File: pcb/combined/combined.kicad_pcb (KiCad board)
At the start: 2 copper layers, 113.5 x 87.5 mm, 67 parts, among them J1 5V POWER, J10 PRESSURE, J11 XIAO D0-D6, J12 XIAO D7-5V, J2 MAINS_IN, J3 VALVE, J4 PUMP, J5 CAN BUS, J6 FLOW HALL, J8 BOILER SSR, Q1 SS8050, Q2 BT136S, Q3 SS8050, Q4 BT136S, Q5 AO3401A, Q6 2N7002, U1 MOC3043M, U2 MOC3023M, U3 EL817C, U4 TJA1051T/3, U5 TMP102AIDRLR, U6 ADS1115IDGSR

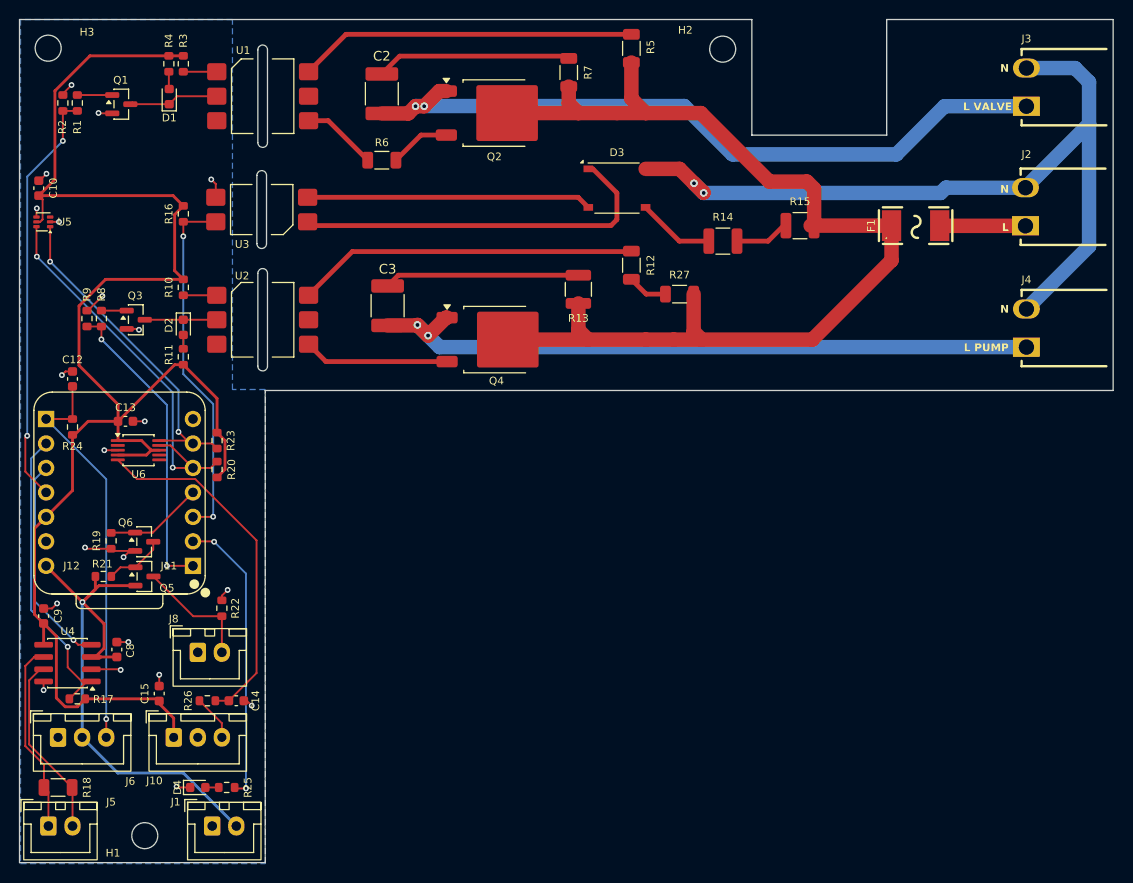
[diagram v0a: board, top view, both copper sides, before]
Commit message: small adjustment to combined PCB
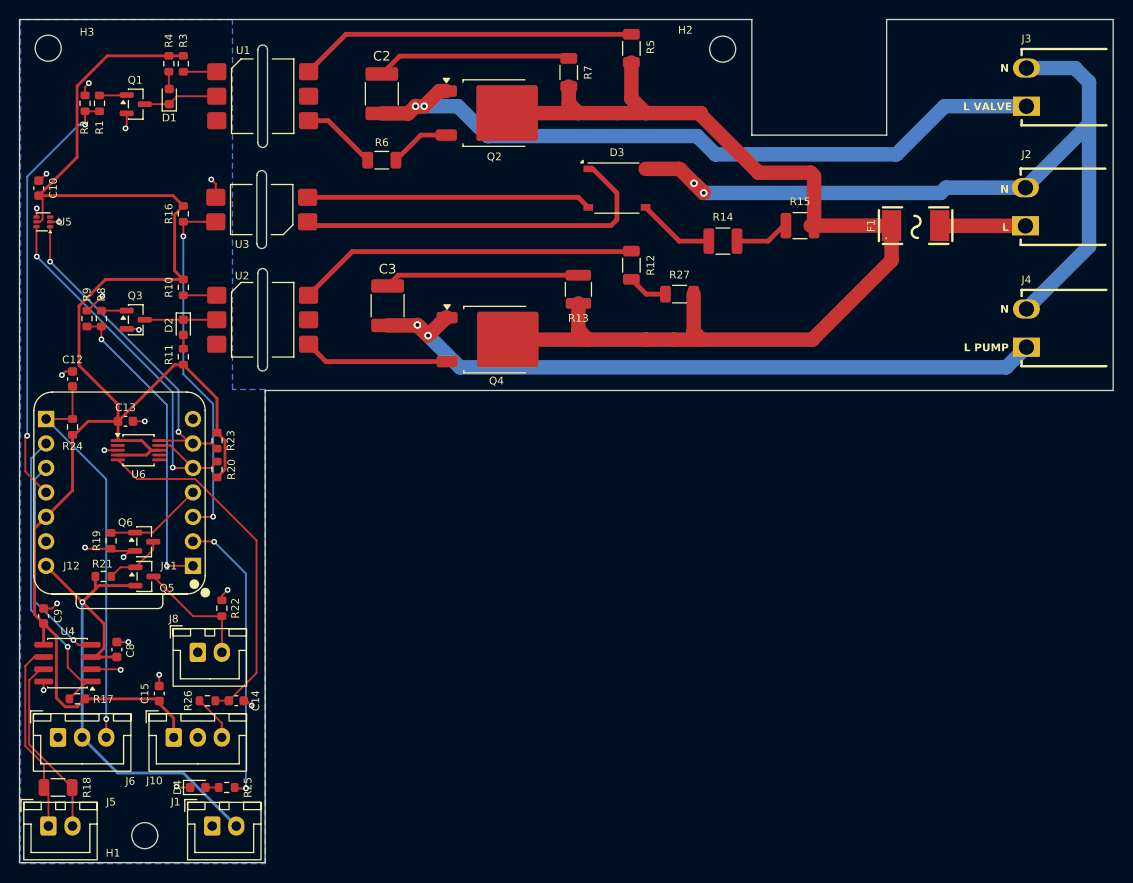
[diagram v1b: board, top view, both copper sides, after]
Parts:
- moved R1 2.30 mm to (88.8, 55.7)
- moved R2 2.30 mm to (87.3, 55.7)
- moved Q1 1.50 mm to (92.6, 55.8)
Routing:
- net Net-(D1-K): track 9.61 -> 7.81 mm
- net /L_PUMP: track 71.6 -> 73.3 mm
- net SSR: track 43.6 -> 44.9 mm
- net +3V3: track 166.1 -> 165.1 mm
- net /L: track 112.5 -> 113.3 mm
- net Net-(Q1-B): track 3.62 -> 2.84 mm
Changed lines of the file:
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@@
 	(footprint "Package_TO_SOT_SMD:SOT-23"
 		(layer "F.Cu")
-		(at 91.0625 55.7875)
+		(at 92.5625 55.7875)
 		(descr "SOT, 3 Pin (JEDEC TO-236 Var AB https://www.jedec.org/document_search?search_api_views_fulltext=TO-236)")
 		(tags "SOT TO_SOT_SMD")
@@
 	(footprint "Resistor_SMD:R_0603_1608Metric"
 		(layer "F.Cu")
-		(at 86.5 55.6625 90)
+		(at 88.8 55.7 90)
 		(descr "Resistor SMD 0603 (1608 Metric), square (rectangular) end terminal, IPC-7351 nominal, (Body size source: IPC-SM-782 page 72, https://www.pcb-3d.com/wordpress/wp-content/uploads/ipc-sm-782a_amendment_1_and_2.pdf)")
 		(tags "resistor")
@@
 	(footprint "Resistor_SMD:R_0603_1608Metric"
 		(layer "F.Cu")
-		(at 85 55.6625 90)
+		(at 87.3 55.7 90)
 		(descr "Resistor SMD 0603 (1608 Metric), square (rectangular) end terminal, IPC-7351 nominal, (Body size source: IPC-SM-782 page 72, https://www.pcb-3d.com/wordpress/wp-content/uploads/ipc-sm-782a_amendment_1_and_2.pdf)")
 		(tags "resistor")
@@
 	)
 	(segment
+		(start 91.625 58.175)
+		(end 91.5 58.3)
+		(width 0.2)
+		(layer "F.Cu")
+		(net "GND")
+	)
+	(segment
 		(start 100.87 64.07)
 		(end 100.4 63.6)
@@
 	)
 	(segment
-		(start 88.7375 56.7375)
-		(end 88.7 56.7)
-		(width 0.2)
-		(layer "F.Cu")
-		(net "GND")
-	)
-	(segment
 		(start 92.5 102.15)
 		(end 90.225 102.15)
@@
 	)
 	(segment
-		(start 85 54.8375)
-		(end 85 54.7)
-		(width 0.2)
-		(layer "F.Cu")
-		(net "GND")
-	)
-	(segment
 		(start 86 83.525)
 		(end 85.275 83.525)
@@
 	)
 	(segment
+		(start 87.3 54.875)
+		(end 87.3 54)
+		(width 0.2)
+		(layer "F.Cu")
+		(net "GND")
+	)
+	(segment
 		(start 83 115.7)
 		(end 83 116.6)
@@
 	)
 	(segment
-		(start 85 54.7)
-		(end 85.9 53.8)
-		(width 0.2)
-		(layer "F.Cu")
-		(net "GND")
-	)
-	(segment
 		(start 101.5 106.8)
 		(end 102.1 106.2)
@@
 	)
 	(segment
-		(start 90.125 56.7375)
-		(end 88.7375 56.7375)
-		(width 0.2)
-		(layer "F.Cu")
-		(net "GND")
-	)
-	(segment
 		(start 82.2575 66.6375)
 		(end 82.295 66.6)
@@
 	)
 	(segment
+		(start 91.625 56.7375)
+		(end 91.625 58.175)
+		(width 0.2)
+		(layer "F.Cu")
+		(net "GND")
+	)
+	(segment
 		(start 101.5 107.275)
 		(end 101.5 106.8)
@@
 	)
 	(segment
+		(start 87.3 54)
+		(end 87.7 53.6)
+		(width 0.2)
+		(layer "F.Cu")
+		(net "GND")
+	)
+	(segment
 		(start 82.5 63.725)
 		(end 82.575 63.725)
@@
 	)
 	(via
-		(at 85.9 53.8)
+		(at 91.5 58.3)
 		(size 0.6)
 		(drill 0.3)
@@
 	)
 	(via
-		(at 88.7 56.7)
-		(size 0.6)
-		(drill 0.3)
-		(layers "F.Cu" "B.Cu")
-		(net "GND")
-	)
-	(via
 		(at 100.4 63.6)
 		(size 0.6)
@@
 	)
 	(via
+		(at 87.7 53.6)
+		(size 0.6)
+		(drill 0.3)
+		(layers "F.Cu" "B.Cu")
+		(net "GND")
+	)
+	(via
 		(at 93.5 88.7)
 		(size 0.6)
@@
 	)
 	(segment
-		(start 90.125 54.8375)
-		(end 86.5 54.8375)
+		(start 88.8 54.875)
+		(end 91.5875 54.875)
 		(width 0.2)
 		(layer "F.Cu")
@@
 	)
 	(segment
-		(start 92.2125 55.575)
-		(end 92 55.7875)
+		(start 91.5875 54.875)
+		(end 91.625 54.8375)
 		(width 0.2)
 		(layer "F.Cu")
-		(net "Net-(D1-K)")
+		(net "Net-(Q1-B)")
 	)
 	(segment
-		(start 100.97 54.96)
-		(end 96.8675 54.96)
+		(start 96.04 55.7875)
+		(end 93.5 55.7875)
 		(width 0.2)
 		(layer "F.Cu")
@@
 	)
 	(segment
-		(start 96.04 55.7875)
-		(end 92 55.7875)
+		(start 100.97 54.96)
+		(end 96.8675 54.96)
 		(width 0.2)
 		(layer "F.Cu")
@@
 	)
 	(segment
+		(start 157.2 62.9)
+		(end 151.21 56.91)
+		(width 1.5)
+		(layer "F.Cu")
+		(net "/L")
+	)
+	(segment
 		(start 137.5 55.71)
 		(end 138.5 56.71)
@@
 	)
 	(segment
-		(start 151.21 56.71)
-		(end 158.3175 63.8175)
+		(start 151.21 56.91)
+		(end 151.21 56.71)
 		(width 1.5)
 		(layer "F.Cu")
@@
 	)
 	(segment
-		(start 158.3175 63.8175)
-		(end 162.2175 63.8175)
+		(start 162.9625 68.3925)
+		(end 162.9625 63.2625)
 		(width 1.5)
 		(layer "F.Cu")
@@
 	)
 	(segment
-		(start 150.4625 75.5)
-		(end 150.4625 79.3825)
+		(start 162.9625 63.2625)
+		(end 162.6 62.9)
 		(width 1.5)
 		(layer "F.Cu")
@@
 	)
 	(segment
-		(start 162.2175 63.8175)
-		(end 162.9625 64.5625)
+		(start 150.4625 75.5)
+		(end 150.4625 79.3825)
 		(width 1.5)
 		(layer "F.Cu")
@@
 	)
 	(segment
-		(start 162.9625 64.5625)
-		(end 162.9625 68.3925)
+		(start 162.6 62.9)
+		(end 157.2 62.9)
 		(width 1.5)
 		(layer "F.Cu")
@@
 	)
 	(segment
-		(start 84.175 63.6)
-		(end 84.175 54.404142)
-		(width 0.3)
-		(layer "F.Cu")
-		(net "+3V3")
-	)
-	(segment
 		(start 90.725 90.675)
 		(end 90.7 90.7)
@@
 	)
 	(segment
-		(start 87.809142 50.77)
-		(end 96 50.77)
-		(width 0.3)
-		(layer "F.Cu")
-		(net "+3V3")
-	)
-	(segment
 		(start 87.62 88.7)
 		(end 90.725 88.7)
@@
 	)
 	(segment
+		(start 86.475 61.3)
+		(end 86.475 53.905761)
+		(width 0.3)
+		(layer "F.Cu")
+		(net "+3V3")
+	)
+	(segment
 		(start 89.43 73.97)
 		(end 97.5 73.97)
@@
 	)
 	(segment
-		(start 82.5 65.275)
-		(end 84.175 63.6)
+		(start 86.475 53.905761)
+		(end 89.610761 50.77)
 		(width 0.3)
 		(layer "F.Cu")
@@
 	)
 	(segment
-		(start 84.175 54.404142)
-		(end 87.809142 50.77)
-		(width 0.3)
-		(layer "F.Cu")
-		(net "+3V3")
-	)
-	(segment
 		(start 101 86.325)
 		(end 101 89.875)
@@
 	)
 	(segment
+		(start 89.610761 50.77)
+		(end 96 50.77)
+		(width 0.3)
+		(layer "F.Cu")
+		(net "+3V3")
+	)
+	(segment
 		(start 96.6 73.07)
 		(end 97.5 73.97)
@@
 	)
 	(segment
+		(start 82.5 65.275)
+		(end 86.475 61.3)
+		(width 0.3)
+		(layer "F.Cu")
+		(net "+3V3")
+	)
+	(segment
 		(start 83.26 98.62)
 		(end 82.06 99.82)
@@
 	)
 	(segment
-		(start 124.1 81)
+		(start 126.2 83.1)
+		(end 182.9 83.1)
+		(width 1.5)
+		(layer "B.Cu")
+		(net "/L_PUMP")
+	)
+	(segment
+		(start 182.9 83.1)
 		(end 185 81)
 		(width 1.5)
@@
 	(segment
 		(start 121.8 78.7)
-		(end 124.1 81)
+		(end 126.2 83.1)
 		(width 1.5)
 		(layer "B.Cu")
@@
 	)
 	(segment
-		(start 86.5 56.4875)
-		(end 85 56.4875)
+		(start 83.26 96.08)
+		(end 81.1 93.92)
 		(width 0.2)
 		(layer "F.Cu")
@@
 	)
 	(segment
-		(start 85 59.6)
-		(end 85 56.4875)
+		(start 81.1 90.4)
+		(end 81.3 90.2)
 		(width 0.2)
 		(layer "F.Cu")
@@
 	)
 	(segment
-		(start 83.26 96.08)
-		(end 81.1 93.92)
+		(start 87.3 57.9)
+		(end 87.3 56.525)
 		(width 0.2)
 		(layer "F.Cu")
@@
 	)
 	(segment
-		(start 81.1 90.4)
-		(end 81.3 90.2)
+		(start 87.3 56.525)
+		(end 88.8 56.525)
 		(width 0.2)
 		(layer "F.Cu")
@@
 	)
 	(via
-		(at 85 59.6)
+		(at 87.3 57.9)
 		(size 0.6)
 		(drill 0.3)
@@
 	(segment
 		(start 81.3 63.3)
-		(end 85 59.6)
+		(end 86.7 57.9)
+		(width 0.2)
+		(layer "B.Cu")
+		(net "SSR")
+	)
+	(segment
+		(start 86.7 57.9)
+		(end 87.3 57.9)
 		(width 0.2)
 		(layer "B.Cu")
@@
 	)
 	(segment
-		(start 154.5 61)
-		(end 149.48 55.98)
+		(start 152.73259 61)
+		(end 150.83259 59.1)
 		(width 1.5)
 		(layer "B.Cu")
@@
 	)
 	(segment
-		(start 176.5 56)
-		(end 171.5 61)
+		(start 171.5 61)
+		(end 152.73259 61)
 		(width 1.5)
 		(layer "B.Cu")
@@
 	)
 	(segment
-		(start 171.5 61)
-		(end 154.5 61)
+		(start 150.83259 59.1)
+		(end 129.1 59.1)
 		(width 1.5)
 		(layer "B.Cu")
@@
 	)
 	(segment
-		(start 149.48 55.98)
-		(end 121.62 55.98)
+		(start 126 56)
+		(end 121.6 56)
+		(width 1.5)
+		(layer "B.Cu")
+		(net "/L_VALVE")
+	)
+	(segment
+		(start 129.1 59.1)
+		(end 126 56)
+		(width 1.5)
+		(layer "B.Cu")
+		(net "/L_VALVE")
+	)
+	(segment
+		(start 176.5 56)
+		(end 171.5 61)
 		(width 1.5)
 		(layer "B.Cu")
